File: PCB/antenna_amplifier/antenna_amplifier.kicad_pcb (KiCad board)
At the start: 4 copper layers, 200 x 100 mm, 134 parts, among them J101 PWR_IN 9V, J201 FILT_IN, J202 BIAS, J401 AES3 OUT, J402 S/PDIF OUT, SW301 RESET, SW302 PCM1804 MODE, SW401 CS8406 MODE, U101 ADM7150ARDZ-5.0, U102 ADM7150ARDZ-3.3, U201 LMP7721, U202 LMP7715, U203 LMP7715, U301 LMP7715, U302 PCM1804, U401 CS8406, Y401 24.576MHz, Y402 24.576MHz

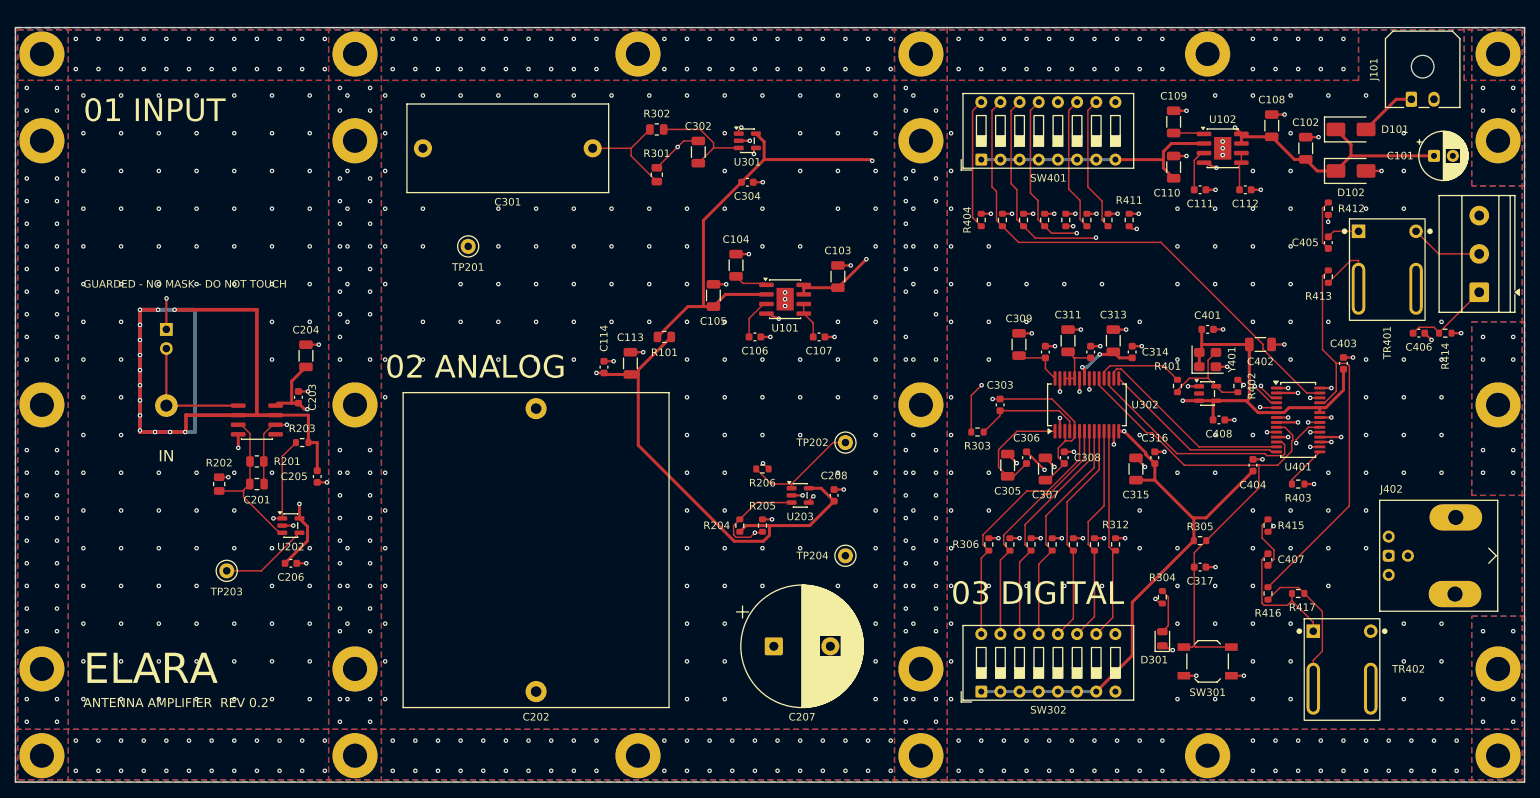
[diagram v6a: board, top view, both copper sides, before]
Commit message: Pedantic schematic and silkscreen pass: zero overlaps, labels clear of tracks
Schematics
- tools/kicadgen/schcheck.py checks KiCad's own SVG rendering (exact stroke boxes)
  for text over text, lines through text, crowded twin labels and text outside the
  frame. Both schematics: 0 findings; ERC 0 on both.
- Generator: Sheet.join (one wire + one label instead of two facing labels),
  per-symbol field positions, per-pin stub lengths, shared power symbol for
  adjacent top/bottom rail pins, crowded rail runs get one label, longer PCM1804
  pins (no-connect cross clear of the pin number), PE value clear of its symbol.
- Fixed: doubled VIN_RAW/BIAS_DIV/LED_OVF/CV_ADJ/LED_C labels, +5VA vs VREG,
  +5V_PRE twins, CS8406 GND straps vs neighbours, BNC/LED/diode fields over their
  graphics, bucket-cell values vs tap labels, notes outside the frame, J2 -> J202.
- Root sheet: sub-sheets in signal-flow order with arrows and a design summary;
  dated title blocks.

Boards
- References prefer spots clear of tracks as well as parts (two candidate rings);
  compartment labels are re-placed after routing; the title block on the back is
  placed as one unit; no stitching via under any board text.
- DRC with schematic parity: amplifier 0 errors / 0 unconnected / 0 parity (only
  the intended bare-island mask warnings); PSU and plate 0 of anything.

Co-Authored-By: Claude Opus 5.5 <noreply@anthropic.com>
Claude-Session: https://claude.ai/code/session_01RsM1DhHhY1tSr2aHjVygSC
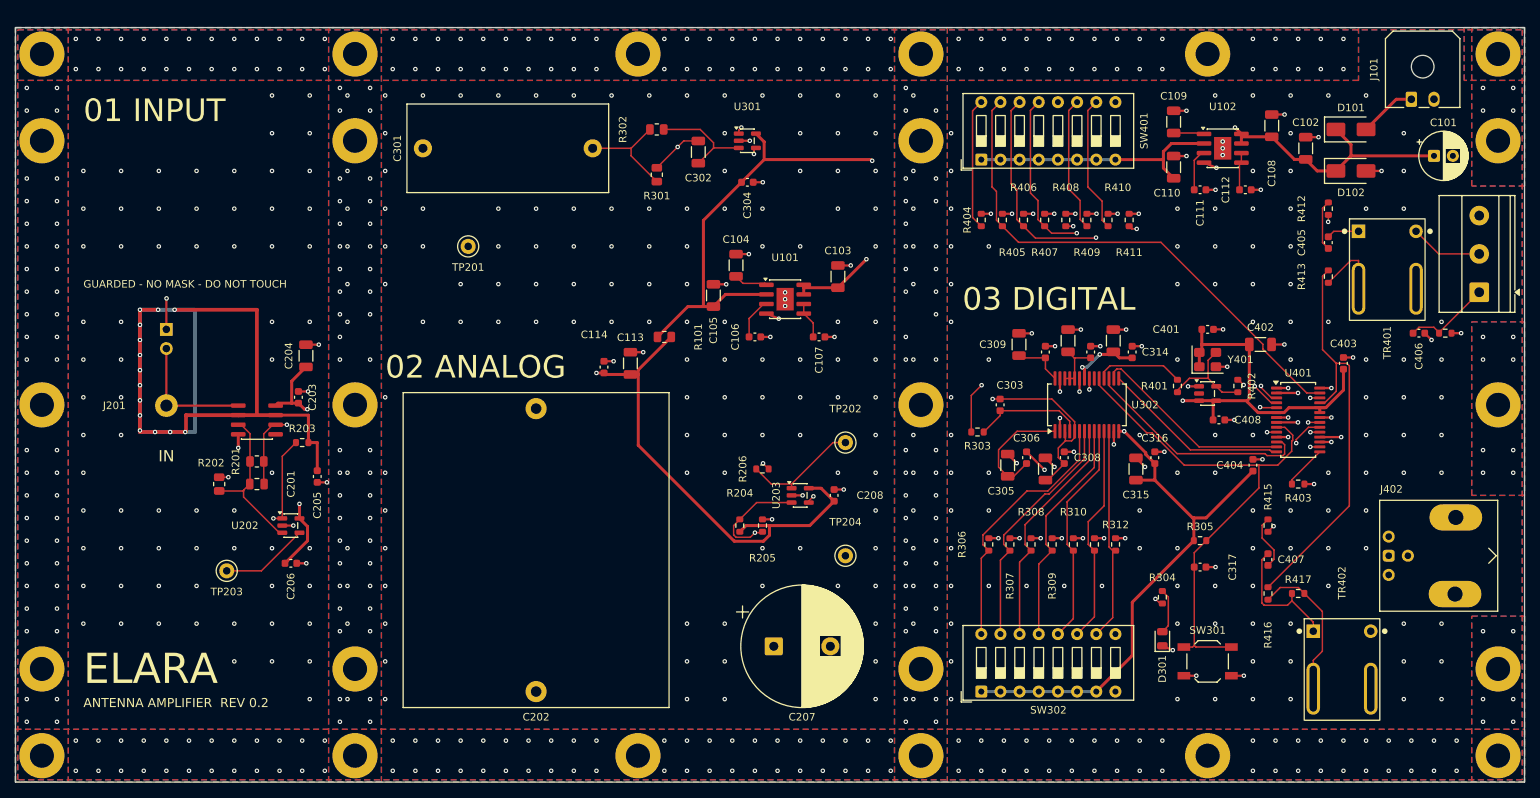
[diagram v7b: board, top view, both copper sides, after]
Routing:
- net GND: vias 788 -> 738

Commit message: Amplifier: single BNC, pluggable AES3, real 63 V Cg, wall clearances
From the placement and parts audit:
- J402 was an Amphenol 031-6575, a dual stacked BNC 29 mm tall that
  could never pass the 14 mm wall notch. Now a single right-angle
  B6252HB-NPP3G-50 (KiCad model), body inside the compartment and
  only the nut/barrel through the notch.
- J401's screw terminals sat under the right wall (screws at x = 194,
  wall from 193) and the shield mounts lid-down, so the AES3 cable could
  not be wired in place. Now a Phoenix MC 1,5/3-G-3,81 right-angle
  header: the MC 1,5/3-ST-3,81 plug is wired outside and pushed in
  through the notch (16 x 13 mm).
- C202's order code was the 100 VDC WIMA (24 x 45.5 mm) on a 35 mm
  footprint. Now MKS4C061007G00KSSD (63 VDC, 41.5 x 20 x 39.5 mm) on the
  matching footprint; C301 on its real 8.5 mm footprint.
- J101 moved 1.5 mm so its body is centred in its notch (was 0.6 mm
  from the notch side); C101, C205 and TR402 moved off the walls.
- ANT_BIAS leaves the island stub through a via so it can reach In2.
- Fab-layer values hidden on both boards: the assembly drawing now shows
  clean references (values are in the BOMs). The STEP export uses the
  board corner as origin for the mechanical fit checks.
DRC: amplifier 77 intended island mask bridges only, PSU 0; unconnected
0 and parity 0 on both; ERC 0; schematic legibility 0.

Co-Authored-By: Claude Opus 5.5 <noreply@anthropic.com>
Claude-Session: https://claude.ai/code/session_01RsM1DhHhY1tSr2aHjVygSC
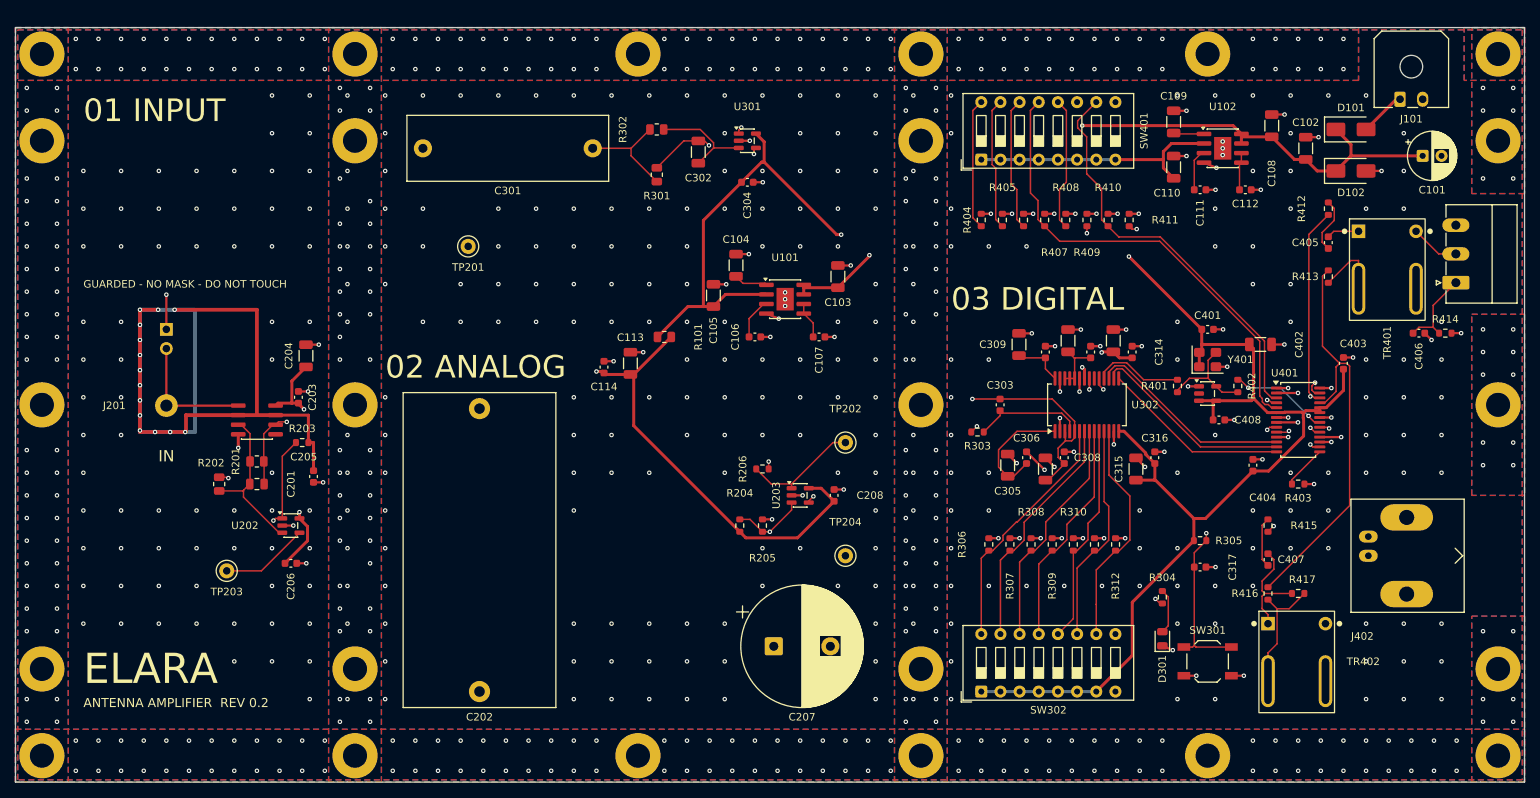
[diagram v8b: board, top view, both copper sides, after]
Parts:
- C202: footprint Capacitor_THT:C_Rect_L41.5mm_W35.0mm_P37.50mm_MKS4 -> Capacitor_THT:C_Rect_L41.5mm_W20.0mm_P37.50mm_MKS4
- C301: footprint Capacitor_THT:C_Rect_L26.5mm_W11.5mm_P22.50mm_MKS4 -> Capacitor_THT:C_Rect_L26.5mm_W8.5mm_P22.50mm_MKS4
- J401: footprint TerminalBlock_Phoenix:TerminalBlock_Phoenix_MKDS-1,5-3-5.08_1x03_P5.08mm_Horizontal -> Connector_Phoenix_MC:PhoenixContact_MC_1,5_3-G-3.81_1x03_P3.81mm_Horizontal
- J402: footprint Connector_Coaxial:BNC_Amphenol_031-6575_Horizontal -> Connector_Coaxial:BNC_Amphenol_B6252HB-NPP3G-50_Horizontal
- moved C202 7.50 mm to (111.5, 138.0)
- moved TR402 6.08 mm to (216.0, 129.0)
- moved J401 3.35 mm to (240.9, 83.8)
- moved J402 2.70 mm to (229.3, 120.0)
- moved C101 1.50 mm to (236.5, 67.0)
- moved J101 1.50 mm to (233.5, 59.5)
- moved C205 0.50 mm to (89.5, 109.5)
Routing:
- net /Clock and S/PDIF + AES3 output/APMS: track 57.6 -> 80.8 mm, vias 2 -> 1
- net /Clock and S/PDIF + AES3 output/SFMT0: track 60.9 -> 79.8 mm, vias 2 -> 1
- net /Clock and S/PDIF + AES3 output/HWCK1: track 69.1 -> 85.8 mm, vias 0 -> 1
- net /Clock and S/PDIF + AES3 output/CEN: track 78.6 -> 62.1 mm, vias 1 -> 2
- net +3V3: track 205.4 -> 191.6 mm, vias 2 -> 1
- net +9V: track 113.8 -> 101.0 mm
- net /Clock and S/PDIF + AES3 output/EMPH_N: track 67.5 -> 54.7 mm, vias 1 -> 0
- net /Clock and S/PDIF + AES3 output/SPDIF_RET: track 22.1 -> 34.5 mm
- net RESET_N: track 70.2 -> 61.4 mm, vias 0 -> 3
- net +5V_PRE: track 138.3 -> 130.8 mm
- net /Electrometer front end/CG: track 53.8 -> 46.3 mm
- net /Clock and S/PDIF + AES3 output/HWCK0: track 89.1 -> 95.3 mm
- net /Electrometer front end/BIAS_DIV: track 30.5 -> 25.1 mm
- net /Clock and S/PDIF + AES3 output/SFMT1: track 58.4 -> 62.9 mm, vias 2 -> 0
- net /Clock and S/PDIF + AES3 output/COAX_P2: track 19.9 -> 16.3 mm
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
